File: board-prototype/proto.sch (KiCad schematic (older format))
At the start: 31 parts

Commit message: Swapped out Am2908s for DS8641s and split the DAL signals to separate T and R.
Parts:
- removed B?: QBUS, symbol QBUS
- removed U? (x6): Am2908, symbol Am2908
- removed U? (x3): 74LVC7T245, symbol 74LVC7T245
- added B101: QBUS, symbol QBUS
- added U101, U102, U103, U110, U111, U112: 74LVC7T245, symbol 74LVC7T245
- added U104, U105, U106, U107, U108, U109: DS8641, symbol DS8641
- gave numbers to parts that had none: 21
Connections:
- net labels added: RBS7, RDAL0, RDAL1, RDAL10, RDAL11, RDAL12, RDAL13, RDAL14, RDAL15, RDAL16, RDAL17, RDAL18, RDAL19, RDAL2, RDAL20, RDAL21, RDAL3, RDAL4, RDAL5, RDAL6, RDAL7, RDAL8, RDAL9, RWTBT, TBS7, TDAL0, TDAL1, TDAL10, TDAL11, TDAL12, TDAL13, TDAL14, TDAL15, TDAL16, TDAL17, TDAL18, TDAL19, TDAL2, TDAL20, TDAL21, TDAL3, TDAL4, TDAL5, TDAL6, TDAL7, TDAL8, TDAL9, TWTBT
- net labels removed: BDALen, DALlatch, DALstrobe, DALtx, RDALen, ZBS7, ZBTWT, ZDAL0, ZDAL1, ZDAL10, ZDAL11, ZDAL12, ZDAL13, ZDAL14, ZDAL15, ZDAL16, ZDAL17, ZDAL18, ZDAL19, ZDAL2, ZDAL20, ZDAL21, ZDAL3, ZDAL4, ZDAL5, ZDAL6, ZDAL7, ZDAL8, ZDAL9, ZDALen
- wire segments 288 -> 303
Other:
- note added: "NOTES:\n\n1) Which signal goes to which package has not yet been fixed. Will be done \n during PCB layout.\n2) Need to add 3.3V regulator.\n3) Do we need to tie the unconnected bus lines on the DS8641s to +5V?"
- note removed: "NOTES:\n\n1) Need to evaluate the various *en signals on the BDAL lines to minimize \n them.\n2) Which signal goes to which package has not yet been fixed. Will be done \n during PCB layout.\n3) Need to add 3.3V regulator.\n4) Do we need to tie the unconnected bus lines on the DS8641s to +5V?"
- moved on the sheet: R101, R102, R103, R104, R105, R106, R107, R108

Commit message: Back to a bidirectional DAL bus.
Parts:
- removed U101, U102, U103: 74LVC7T245, symbol 74LVC7T245
- removed U117, U118, U119: DS8641, symbol DS8641
- added U101, U102, U103: DS8641, symbol DS8641
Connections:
- net labels added: ZBS7, ZDAL0, ZDAL1, ZDAL10, ZDAL11, ZDAL12, ZDAL13, ZDAL14, ZDAL15, ZDAL16, ZDAL17, ZDAL18, ZDAL19, ZDAL2, ZDAL20, ZDAL21, ZDAL3, ZDAL4, ZDAL5, ZDAL6, ZDAL7, ZDAL8, ZDAL9, ZWTBT, ~DALtx
- net labels removed: RBS7, RDAL0, RDAL1, RDAL10, RDAL11, RDAL12, RDAL13, RDAL14, RDAL15, RDAL16, RDAL17, RDAL18, RDAL19, RDAL2, RDAL20, RDAL21, RDAL3, RDAL4, RDAL5, RDAL6, RDAL7, RDAL8, RDAL9, RWTBT, TBS7, TDAL0, TDAL1, TDAL10, TDAL11, TDAL12, TDAL13, TDAL14, TDAL15, TDAL16, TDAL17, TDAL18, TDAL19, TDAL2, TDAL20, TDAL21, TDAL3, TDAL4, TDAL5, TDAL6, TDAL7, TDAL8, TDAL9, TWTBT
- wire segments 303 -> 248
- no-connect marks 36 -> 40
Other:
- moved on the sheet: C101, C102, R101, R102, R103, R104, R105, R106, R107, R108, U110, U111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

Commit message: Full circle, back to using Am2908s and a bidirectional DAL bus.  Fixed a few other things along the way, like sorting out the direction and strobe lines and adding level shifting for them.
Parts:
- removed U101, U102, U103, U104, U105, U106: DS8641, symbol DS8641
- added U101, U102, U103, U104, U105, U106: Am2908, symbol Am2908
- renumbered U110 to U107, U111 to U108, U112 to U109, U107 to U110, U108 to U111, U109 to U112, U115 to U113, U116 to U114, U113 to U115, U120 to U116, U114 to U117, U121 to U118, U122 to U119, U123 to U120
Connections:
- net labels added: DALst
- wire segments 248 -> 329
- no-connect marks 40 -> 36
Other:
- moved on the sheet: U107, U108, U109

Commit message: Separate some of the control signals for the BDAL lines.
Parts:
- removed U110, U111, U112, U113, U114: DS8641, symbol DS8641
- added U? (x5): DS8641-LR, symbol DS8641-LR
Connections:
- net labels added: DALtx, iDALst, iDALtx, ~DALbe, ~iDALbe
- net labels removed: ~DALtx
- wire segments 329 -> 270
- no-connect marks 36 -> 45
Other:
- moved on the sheet: R101, R102, R103, R104, R105, R106, R107, R108, U115, U116, U117, U118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

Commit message: Added connections to ZTEX FPGA module.
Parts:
- added P?: AB, symbol CONN_ZTEX_AB
- added P?: CD, symbol CONN_ZTEX_CD
- added SW?: RESET, symbol SW_PUSH_SMALL
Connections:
- net +5V: now also P?.1 (A1), P?.2 (B1)
- net DALst: now also P?.53 (A27)
- net DALtx: now also P?.51 (A26)
- net GND: now also P?.1 (C1), P?.3 (A2), P?.31 (A16), P?.32 (B16), P?.33 (C17), P?.34 (D17), P?.4 (B2), P?.4 (D2), P?.63 (C32), P?.64 (B32), P?.64 (D32), SW?.2
- net RDCOK: now also P?.47 (C24)
- net RDIN: now also P?.5 (C3)
- net RDMGI: now also P?.49 (C25)
- net RDMR: now also P?.13 (C7)
- net RDOUT: now also P?.7 (C4)
- net RIAKI: now also P?.51 (C26)
- net RINIT: now also P?.37 (C19)
- net RIRQ4: now also P?.15 (C8)
- net RIRQ5: now also P?.17 (C9)
- net RIRQ6: now also P?.19 (C10)
- net RIRQ7: now also P?.21 (C11)
- net RPOK: now also P?.45 (C23)
- net RREF: now also P?.11 (C6)
- net RRPLY: now also P?.9 (C5)
- net RSACK: now also P?.25 (C13)
- net RSYNC: now also P?.3 (C2)
- net TDIN: now also P?.48 (D24)
- net TDMGO: now also P?.60 (D30)
- net TDMR: now also P?.56 (D28)
- net TDOUT: now also P?.50 (D25)
- net TIAKO: now also P?.58 (D29)
- net TIRQ4: now also P?.8 (D4)
- net TIRQ5: now also P?.10 (D5)
- net TIRQ6: now also P?.12 (D6)
- net TIRQ7: now also P?.14 (D7)
- net TREF: now also P?.54 (D27)
- net TRPLY: now also P?.52 (D26)
- net TSACK: now also P?.6 (D3)
- net TSYNC: now also P?.46 (D23)
- net ZBS7: now also P?.47 (A24)
- net ZDAL0: now also P?.10 (B5)
- net ZDAL1: now also P?.12 (B6)
- net ZDAL10: now also P?.25 (A13)
- net ZDAL11: now also P?.26 (B13)
- net ZDAL12: now also P?.27 (A14)
- net ZDAL13: now also P?.28 (B14)
- net ZDAL14: now also P?.35 (A18)
- net ZDAL15: now also P?.36 (B18)
- net ZDAL16: now also P?.39 (A20)
- net ZDAL17: now also P?.40 (B20)
- net ZDAL18: now also P?.41 (A21)
- net ZDAL19: now also P?.42 (B21)
- net ZDAL2: now also P?.13 (A7)
- net ZDAL20: now also P?.45 (A23)
- net ZDAL21: now also P?.46 (B23)
- net ZDAL3: now also P?.14 (B7)
- net ZDAL4: now also P?.15 (A8)
- net ZDAL5: now also P?.16 (B8)
- net ZDAL6: now also P?.17 (A9)
- net ZDAL7: now also P?.19 (A10)
- net ZDAL8: now also P?.21 (A11)
- net ZDAL9: now also P?.23 (A12)
- net ZWTBT: now also P?.48 (B24)
- net ~DALbe: now also P?.55 (A28)
- new net: P?.2 (D1), SW?.1
- no-connect marks 45 -> 74
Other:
- note added: "NOTES:\n\n1) Which signal goes to which package has not yet been fixed.\n Will be done during PCB layout.\n2) Do we need to tie the unconnected bus lines on the\n DS8641s to +5V?"
- note added: "ZTEX Module Connector"
- note removed: "NOTES:\n\n1) Which signal goes to which package has not yet been fixed. Will be done \n during PCB layout.\n2) Need to add 3.3V regulator.\n3) Do we need to tie the unconnected bus lines on the DS8641s to +5V?"
- moved on the sheet: B101, C101, C102, R101, R102, R103, R104, R105, R106, R107, R108, U101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

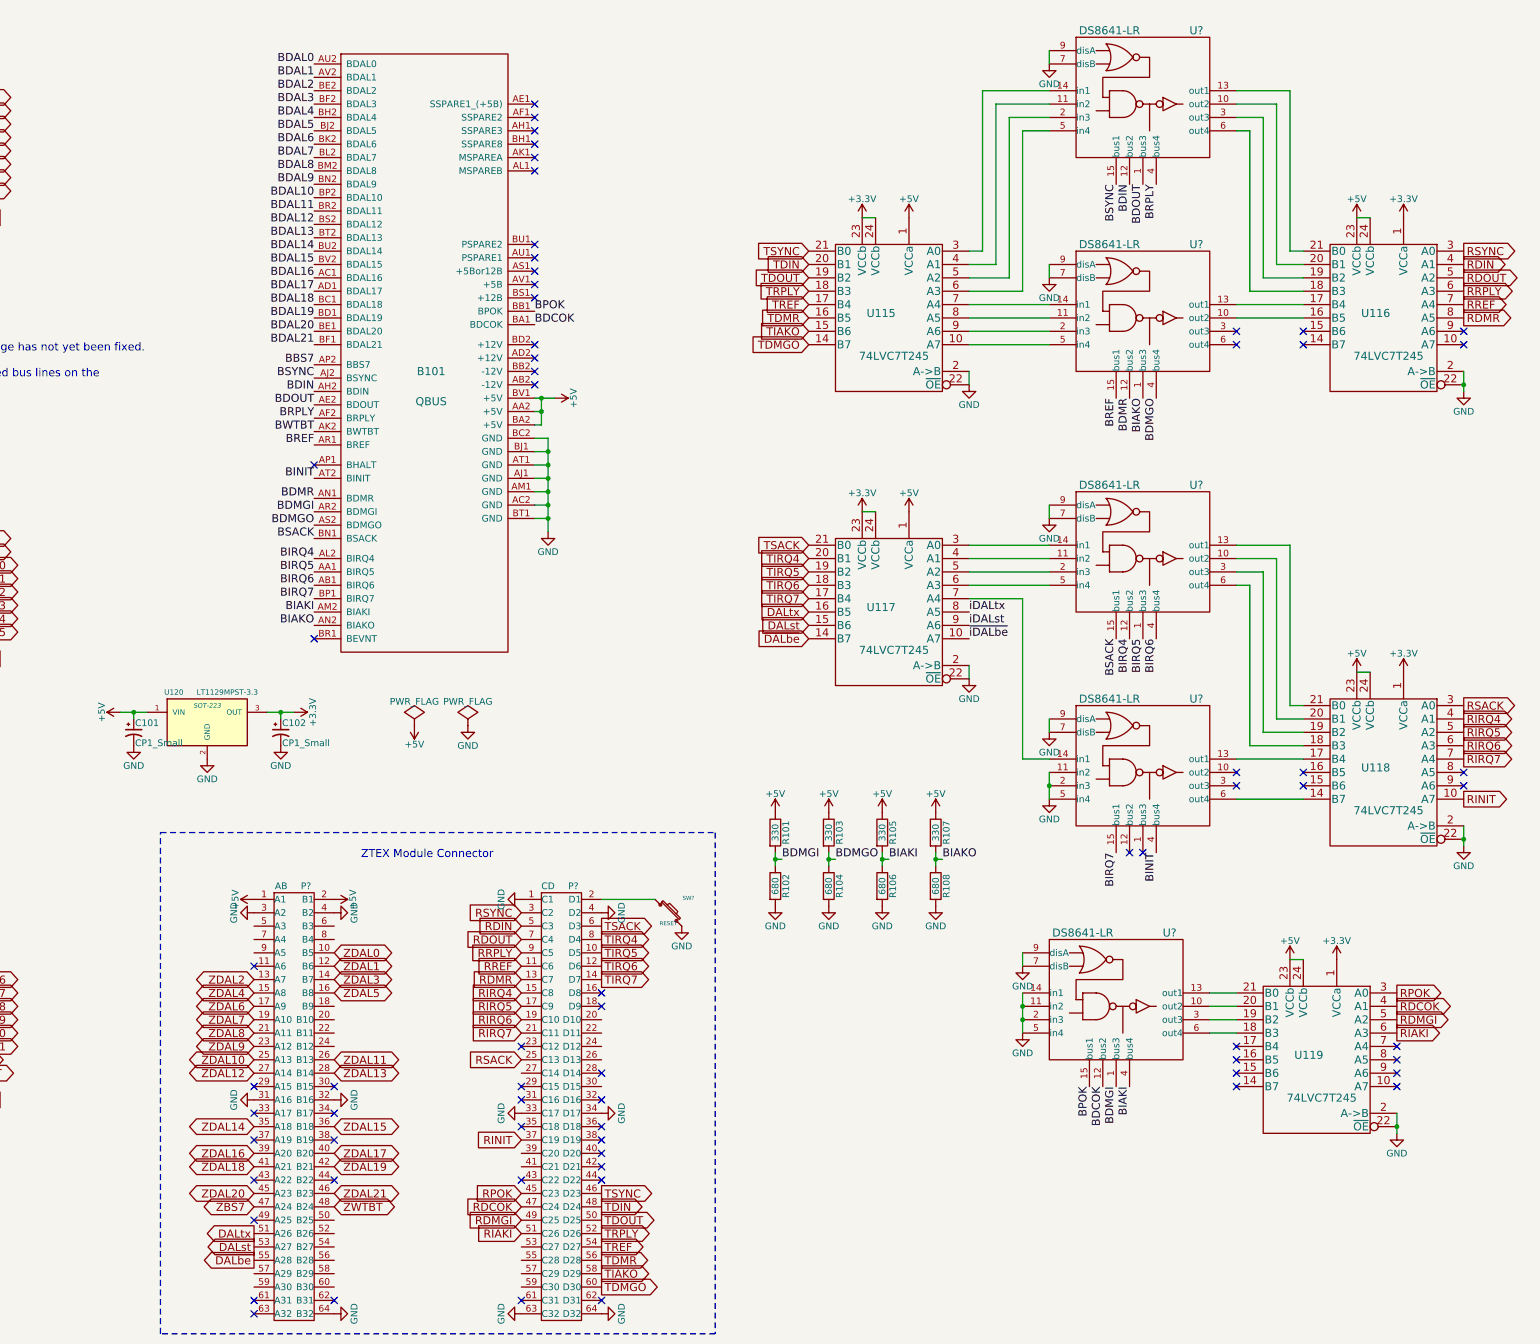
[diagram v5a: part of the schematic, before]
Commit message: Fixed bug with gnd on C1.  Should be C2 and moved RSYNC down to C14.
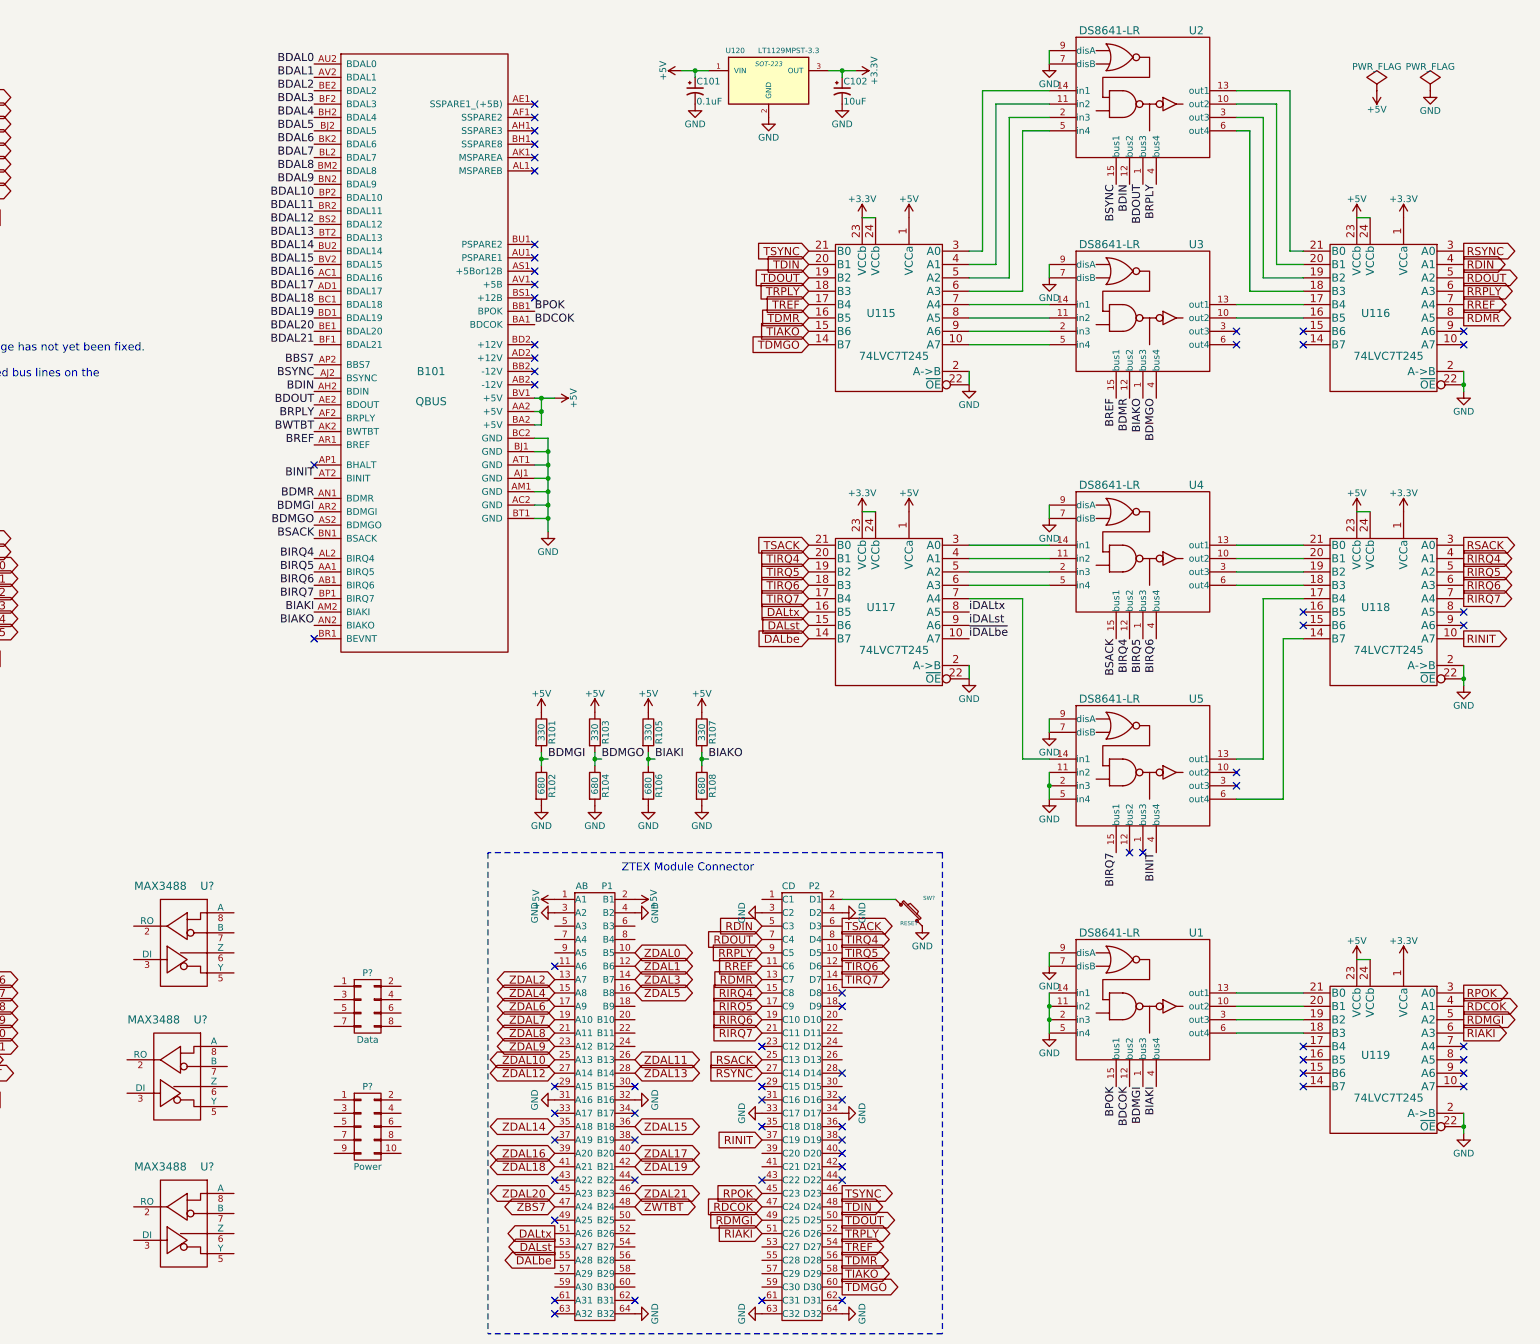
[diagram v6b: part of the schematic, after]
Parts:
- added P?: Data, symbol CONN_02X04
- added P?: Power, symbol CONN_02X05
- added U? (x3): MAX3488, symbol MAX3488
- C101: value CP1_Small -> 0.1uF
- C102: value CP1_Small -> 10uF
- gave numbers to parts that had none: 7
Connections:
- net GND: now also P2.3 (C2), U?.4 (GND), U?.4 (GND), U?.4 (GND); no longer P2.1 (C1)
- net RSYNC: now also P2.27 (C14); no longer P2.3 (C2)
- new net Vdd: U?.1 (Vdd), U?.1 (Vdd), U?.1 (Vdd)
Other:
- moved on the sheet: C101, C102, P1, P2, R101, R102, R103, R104, R105, R106, R107, R108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

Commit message: Moved RSYNC from C14 to B12 so it can be used as a clock.
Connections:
- net GND: now also P?.3 (P3), P?.4 (P4), P?.5 (P5), P?.6 (P6), P?.7 (P7), P?.8 (P8)
- net RSYNC: now also P1.24 (B12); no longer P2.27 (C14)
- net +12V: now reaches B101.AD2 (+12V)
- net +12V: now also B101.BD2 (+12V), P?.1 (P1), P?.10 (P10), P?.2 (P2), P?.9 (P9)
- net IPlatch: now reaches U?.3 (DI)
- net IPlatchN: now reaches U?.5 (Y)
- net IPlatchN: now also P?.8 (P8)
- net IPlatchP: now reaches U?.6 (Z)
- net IPlatchP: now also P?.7 (P7)
- net IPdata: now reaches U?.3 (DI)
- net IPdataN: now reaches U?.5 (Y)
- net IPdataN: now also P?.2 (P2)
- net IPdataP: now reaches U?.6 (Z)
- net IPdataP: now also P?.1 (P1)
- net IPclk: now reaches U?.3 (DI)
- net IPclkN: now reaches U?.5 (Y)
- net IPclkN: now also P?.6 (P6)
- net IPclkP: now reaches U?.6 (Z)
- net IPclkP: now also P?.3 (P3)
- no-connect marks 74 -> 83
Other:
- note added: "Indicator Panel"
- note added: "NOTES:\n\n1) Which signal goes to which package has not yet\n been fixed. Will be done during PCB layout.\n2) Do we need to tie the unconnected bus lines on\n the DS8641s to +5V?"
- note removed: "NOTES:\n\n1) Which signal goes to which package has not yet been fixed.\n Will be done during PCB layout.\n2) Do we need to tie the unconnected bus lines on the\n DS8641s to +5V?"
- moved on the sheet: B101, C101, C102, P?, U104, U107, U108, U109, U120, U?

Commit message: Wirewrap board is now split off, this is the PC prototype.
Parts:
- removed U120: LT1129MPST-3.3, SOT-223, symbol LT1129MPST-3.3
- added C103, C104, C105, C106, C107, C108, C109, C110, C111, C112, C113, C114, C115, C116, C117, C118, C119, C120, C121, C126, C127, C128, C129, C130, C131, C132, C133: 100nF, Capacitors_SMD:C_0805, symbol C_Small
- added U120: LD1117S33CTR, TO_SOT_Packages_SMD:SOT-223, symbol LD1117S33CTR
- B101: footprint (none) -> myMods.pretty:Qbus
- C101: value 0.1uF -> 0.1µF; footprint (none) -> Capacitors_Tantalum_SMD:TantalC_SizeR_EIA-2012
- C102: value 10uF -> 10µF; footprint (none) -> Capacitors_Tantalum_SMD:TantalC_SizeR_EIA-2012
- P1, P2: footprint (none) -> Pin_Headers:Pin_Header_Straight_2x32
- P101: renamed from P?; footprint (none) -> Pin_Headers:Pin_Header_Angled_2x04
- P102: renamed from P?; footprint (none) -> Pin_Headers:Pin_Header_Angled_2x05
- R101, R103, R105, R107: value 330 -> 330Ω; footprint (none) -> Resistors_SMD:R_0805
- R102, R104, R106, R108: value 680 -> 680Ω; footprint (none) -> Resistors_SMD:R_0805
- U101, U106: footprint (none) -> Sockets_DIP:DIP-20__300
- U102: renamed from U104; footprint (none) -> Sockets_DIP:DIP-20__300
- U103: renamed from U102; footprint (none) -> Sockets_DIP:DIP-20__300
- U104: renamed from U105; footprint (none) -> Sockets_DIP:DIP-20__300
- U105: renamed from U103; footprint (none) -> Sockets_DIP:DIP-20__300
- U107, U108, U109, U115, U116, U117, U118, U119: footprint (none) -> SMD_Packages:SOIC-24
- U110, U111, U112: renamed from U?; footprint (none) -> Housings_DIP:DIP-8__300
- U201: renamed from U2; footprint (none) -> Sockets_DIP:DIP-16__300
- U202: renamed from U3; footprint (none) -> Sockets_DIP:DIP-16__300
- U203: renamed from U4; footprint (none) -> Sockets_DIP:DIP-16__300
- U204: renamed from U5; footprint (none) -> Sockets_DIP:DIP-16__300
- U205: renamed from U1; footprint (none) -> Sockets_DIP:DIP-16__300
- gave numbers to parts that had none: 1
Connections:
- net VCC is gone; now on net +5V: U101.20 (VCC), U102.20 (VCC), U103.20 (VCC), U104.20 (VCC), U105.20 (VCC), U106.20 (VCC), U201.16 (VCC), U202.16 (VCC), U203.16 (VCC), U204.16 (VCC), U205.16 (VCC)
- net +3V3: now also C126.1, C127.1, C128.1, C129.1, C130.1, C131.1, C132.1, C133.1, U120.2 (VO)
- net +5V: now also C103.1, C104.1, C105.1, C106.1, C107.1, C108.1, C109.1, C110.1, C111.1, C112.1, C113.1, C114.1, C115.1, C116.1, C117.1, C118.1, C119.1, C120.1, C121.1, U120.3 (VI)
- net BBS7: now also U101.4 (BUS0); no longer U106.14 (BUS2)
- net BDAL0: now also U102.16 (BUS3); no longer U101.4 (BUS0)
- net BDAL1: now also U102.14 (BUS2); no longer U101.6 (BUS1)
- net BDAL10: now also U105.4 (BUS0); no longer U103.14 (BUS2)
- net BDAL11: now also U105.6 (BUS1); no longer U103.16 (BUS3)
- net BDAL12: now also U106.14 (BUS2); no longer U104.4 (BUS0)
- net BDAL13: now also U106.16 (BUS3); no longer U104.6 (BUS1)
- net BDAL14: now also U106.4 (BUS0); no longer U104.14 (BUS2)
- net BDAL15: now also U106.6 (BUS1); no longer U104.16 (BUS3)
- net BDAL16: now also U101.16 (BUS3); no longer U105.4 (BUS0)
- net BDAL17: now also U101.14 (BUS2); no longer U105.6 (BUS1)
- net BDAL18: now also U102.6 (BUS1); no longer U105.14 (BUS2)
- net BDAL19: now also U102.4 (BUS0); no longer U105.16 (BUS3)
- net BDAL2: now also U103.16 (BUS3); no longer U101.14 (BUS2)
- net BDAL20: now also U103.14 (BUS2); no longer U106.4 (BUS0)
- net BDAL21: now also U103.6 (BUS1); no longer U106.6 (BUS1)
- net BDAL3: now also U103.4 (BUS0); no longer U101.16 (BUS3)
- net BDAL4: now also U104.16 (BUS3); no longer U102.4 (BUS0)
- net BDAL5: now also U104.14 (BUS2); no longer U102.6 (BUS1)
- net BDAL6: now also U104.4 (BUS0); no longer U102.14 (BUS2)
- net BDAL7: now also U104.6 (BUS1); no longer U102.16 (BUS3)
- net BDAL8: now also U105.16 (BUS3); no longer U103.4 (BUS0)
- net BDAL9: now also U105.14 (BUS2); no longer U103.6 (BUS1)
- net BDIN: now also U202.12 (bus2); no longer U201.12 (bus2)
- net BDMGI: now also U203.4 (bus4); no longer U205.1 (bus3)
- net BDMGO: now also U204.12 (bus2); no longer U202.4 (bus4)
- net BDMR: now also U203.12 (bus2); no longer U202.12 (bus2)
- net BIAKI: now also U202.4 (bus4); no longer U205.4 (bus4)
- net BIAKO: now also U203.15 (bus1); no longer U202.1 (bus3)
- net BIRQ4: now also U202.1 (bus3); no longer U203.12 (bus2)
- net BIRQ5: now also U201.15 (bus1); no longer U203.1 (bus3)
- net BIRQ6: now also U201.12 (bus2); no longer U203.4 (bus4)
- net BIRQ7: now also U205.4 (bus4); no longer U204.15 (bus1)
- net BREF: now also U203.1 (bus3); no longer U202.15 (bus1)
- net BSACK: now also U205.1 (bus3); no longer U203.15 (bus1)
- net BSYNC: now also U202.15 (bus1); no longer U201.15 (bus1)
- net BWTBT: now also U101.6 (BUS1); no longer U106.16 (BUS3)
- net DALtx: now also U117.18 (B3); no longer U117.16 (B5)
- net GND: now also U202.5 (in4), U203.5 (in4), U204.14 (in1), C103.2, C104.2, C105.2, C106.2, C107.2, C108.2, C109.2, C110.2, C111.2, C112.2, C113.2, C114.2, C115.2, C116.2, C117.2, C118.2, C119.2, C120.2, C121.2, C126.2, C127.2, C128.2, C129.2, C130.2, C131.2, C132.2, C133.2, U120.1 (GND); no longer U204.11 (in2), U205.2 (in3), U205.5 (in4)
- net RDIN: now also U116.8 (A5); no longer U116.4 (A1)
- net RDMGI: now also U118.6 (A3); no longer U119.5 (A2)
- net RDMR: now also U118.4 (A1); no longer U116.8 (A5)
- net RIAKI: now also U116.10 (A7); no longer U119.6 (A3)
- net RIRQ4: now also U116.9 (A6); no longer U118.4 (A1)
- net RIRQ5: now also U116.3 (A0); no longer U118.5 (A2)
- net RIRQ6: now also U116.4 (A1); no longer U118.6 (A3)
- net RIRQ7: now also U119.6 (A3); no longer U118.7 (A4)
- net RREF: now also U118.5 (A2); no longer U116.7 (A4)
- net RSACK: now also U119.5 (A2); no longer U118.3 (A0)
- net RSYNC: now also U116.7 (A4); no longer U116.3 (A0)
- net TDIN: now also U115.16 (B5); no longer U115.20 (B1)
- net TDMGO: now also U117.16 (B5); no longer U115.14 (B7)
- net TDMR: now also U117.20 (B1); no longer U115.16 (B5)
- net TIAKO: now also U117.21 (B0); no longer U115.15 (B6)
- net TIRQ4: now also U115.15 (B6); no longer U117.20 (B1)
- net TIRQ5: now also U115.21 (B0); no longer U117.19 (B2)
- net TIRQ6: now also U115.20 (B1); no longer U117.18 (B3)
- net TIRQ7: now also U115.14 (B7); no longer U117.17 (B4)
- net TREF: now also U117.19 (B2); no longer U115.17 (B4)
- net TSACK: now also U117.17 (B4); no longer U117.21 (B0)
- net TSYNC: now also U115.17 (B4); no longer U115.21 (B0)
- net ZBS7: now also U107.3 (A0); no longer U109.9 (A6)
- net ZDAL0: now also U107.7 (A4); no longer U107.3 (A0)
- net ZDAL1: now also U107.8 (A5); no longer U107.4 (A1)
- net ZDAL10: now also U109.6 (A3); no longer U108.5 (A2)
- net ZDAL11: now also U109.5 (A2); no longer U108.6 (A3)
- net ZDAL12: now also U109.8 (A5); no longer U108.7 (A4)
- net ZDAL13: now also U109.7 (A4); no longer U108.8 (A5)
- net ZDAL14: now also U109.9 (A6); no longer U108.9 (A6)
- net ZDAL15: now also U109.10 (A7); no longer U108.10 (A7)
- net ZDAL16: now also U107.6 (A3); no longer U109.3 (A0)
- net ZDAL17: now also U107.5 (A2); no longer U109.4 (A1)
- net ZDAL18: now also U107.9 (A6); no longer U109.5 (A2)
- net ZDAL19: now also U107.10 (A7); no longer U109.6 (A3)
- net ZDAL2: now also U108.3 (A0); no longer U107.5 (A2)
- net ZDAL20: now also U108.4 (A1); no longer U109.7 (A4)
- net ZDAL21: now also U108.6 (A3); no longer U109.8 (A5)
- net ZDAL3: now also U108.5 (A2); no longer U107.6 (A3)
- net ZDAL4: now also U108.7 (A4); no longer U107.7 (A4)
- net ZDAL5: now also U108.8 (A5); no longer U107.8 (A5)
- net ZDAL6: now also U108.10 (A7); no longer U107.9 (A6)
- net ZDAL7: now also U108.9 (A6); no longer U107.10 (A7)
- net ZDAL8: now also U109.3 (A0); no longer U108.3 (A0)
- net ZDAL9: now also U109.4 (A1); no longer U108.4 (A1)
- net ZWTBT: now also U107.4 (A1); no longer U109.10 (A7)
- net iDALtx: now also U117.6 (A3); no longer U117.8 (A5)
- net at U115.10 (A7): now also U205.2 (in3); no longer U202.5 (in4)
- net at U116.14 (B7): now also U202.6 (out4)
- net at U116.15 (B6): now also U202.3 (out3)
- net at U117.7 (A4): now also U205.5 (in4); no longer U204.14 (in1)
- net at U118.17 (B4): no longer U204.13 (out1)
- net at U118.21 (B0): no longer U203.13 (out1)
- net at U102.17 (A3), U102.18 (R3): now also U107.17 (B4); no longer U107.14 (B7)
- net at U102.12 (R2), U102.13 (A2): now also U107.16 (B5); no longer U107.15 (B6)
- net at U102.7 (A1), U102.8 (R1): now also U107.15 (B6); no longer U107.16 (B5)
- net at U102.2 (R0), U102.3 (A0): now also U107.14 (B7); no longer U107.17 (B4)
- net at U104.17 (A3), U104.18 (R3): now also U108.17 (B4); no longer U108.14 (B7)
- net at U104.12 (R2), U104.13 (A2): now also U108.16 (B5); no longer U108.15 (B6)
- net at U104.7 (A1), U104.8 (R1): now also U108.15 (B6); no longer U108.16 (B5)
- net at U104.2 (R0), U104.3 (A0): now also U108.14 (B7); no longer U108.17 (B4)
- net at U103.17 (A3), U103.18 (R3): now also U108.21 (B0); no longer U108.18 (B3)
- net at U103.12 (R2), U103.13 (A2): now also U108.20 (B1); no longer U108.19 (B2)
- net at U103.7 (A1), U103.8 (R1): now also U108.18 (B3); no longer U108.20 (B1)
- net at U103.2 (R0), U103.3 (A0): now also U108.19 (B2); no longer U108.21 (B0)
- net at U106.17 (A3), U106.18 (R3): now also U109.17 (B4); no longer U109.14 (B7)
- net at U106.12 (R2), U106.13 (A2): now also U109.16 (B5); no longer U109.15 (B6)
- net at U106.7 (A1), U106.8 (R1): now also U109.14 (B7); no longer U109.16 (B5)
- net at U106.2 (R0), U106.3 (A0): now also U109.15 (B6); no longer U109.17 (B4)
- net at U105.17 (A3), U105.18 (R3): now also U109.21 (B0); no longer U109.18 (B3)
- net at U105.12 (R2), U105.13 (A2): now also U109.20 (B1); no longer U109.19 (B2)
- net at U105.7 (A1), U105.8 (R1): now also U109.19 (B2); no longer U109.20 (B1)
- net at U105.2 (R0), U105.3 (A0): now also U109.18 (B3); no longer U109.21 (B0)
- new net: U117.8 (A5), U204.11 (in2)
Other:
- note added: "NOTES:\n\n1) Which signal goes to which package has not yet\n been fixed. Will be done during PCB layout.\n2) Do we need to tie the unconnected bus lines on\n the DS8641s to +5V?\n3) Check that Vcc to the RS422 drivers is the right\n voltage."
- note removed: "NOTES:\n\n1) Which signal goes to which package has not yet\n been fixed. Will be done during PCB layout.\n2) Do we need to tie the unconnected bus lines on\n the DS8641s to +5V?"
- moved on the sheet: C101
